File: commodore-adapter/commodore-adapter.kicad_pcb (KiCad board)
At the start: 2 copper layers, 16 x 14.5 mm, 2 parts, among them CN1 1x9, CN2 1x8

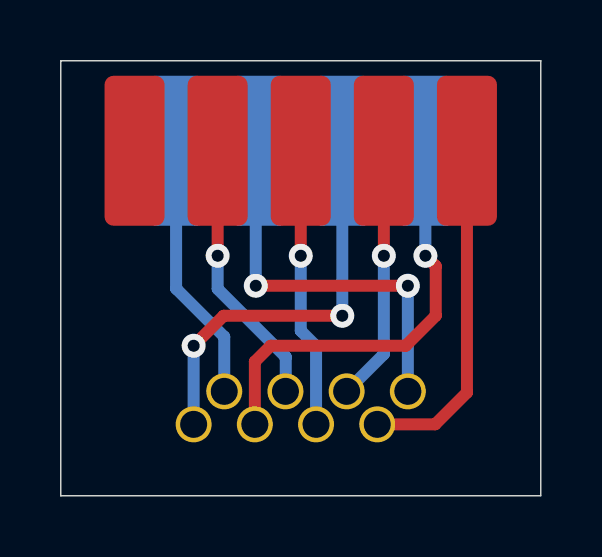
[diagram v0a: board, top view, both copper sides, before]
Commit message: fixed DB9 pinout from male to female
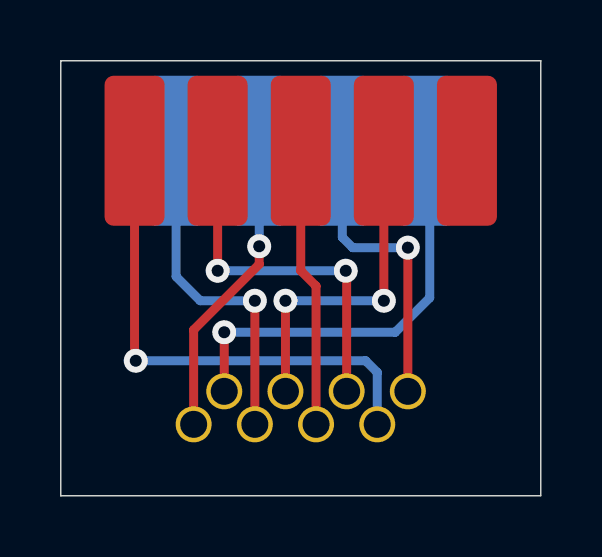
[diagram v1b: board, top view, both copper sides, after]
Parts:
- CN1: footprint d-sub:DB9 board edge -> d-sub:DB9 female board edge
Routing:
- net /b: track 8.68 -> 14.3 mm, vias 0 -> 1
- net /up: track 11.5 -> 17.0 mm, vias 0 -> 1
- net /down: track 8.58 -> 12.3 mm, vias 1 -> 2
- net /5V: track 13.5 -> 10.2 mm, vias 2 -> 1
- net /GND: track 13.2 -> 10.0 mm, vias 2 -> 1
- net /a: track 14.4 -> 11.3 mm
- net /right: track 8.96 -> 11.3 mm, vias 1 -> 2
- net /left: vias 1 -> 0
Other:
- rule pad_to_mask_clearance: 0.051 -> 0
- board text added: "GOOD MICROS"
- board text removed: "GOODMICROS"
